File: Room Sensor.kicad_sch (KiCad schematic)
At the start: 15 parts, among them SW1 SW_Push, SW2 SW_Push, SW3 SW_Push, SW4 SW_Push, U2 ESP32-C3_SUPERMINI_TH

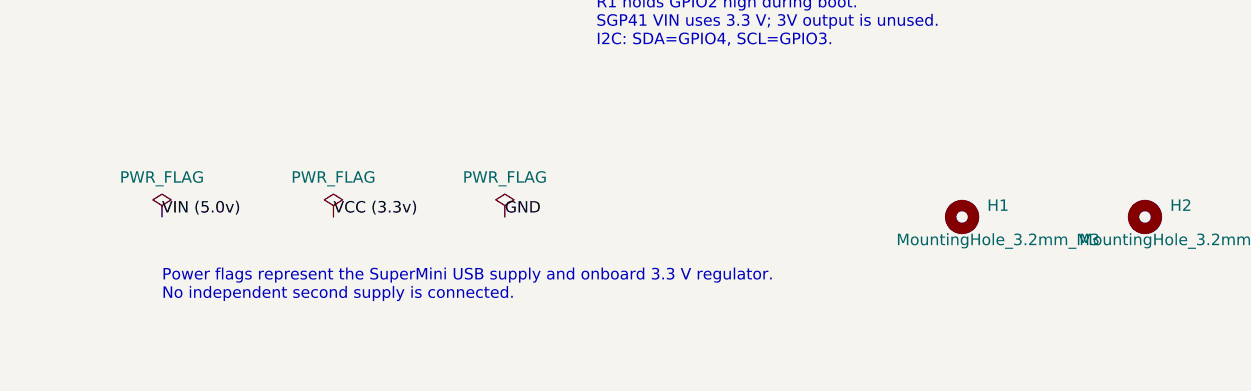
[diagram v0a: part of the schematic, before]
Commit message: Add KiCad latching USB power interface
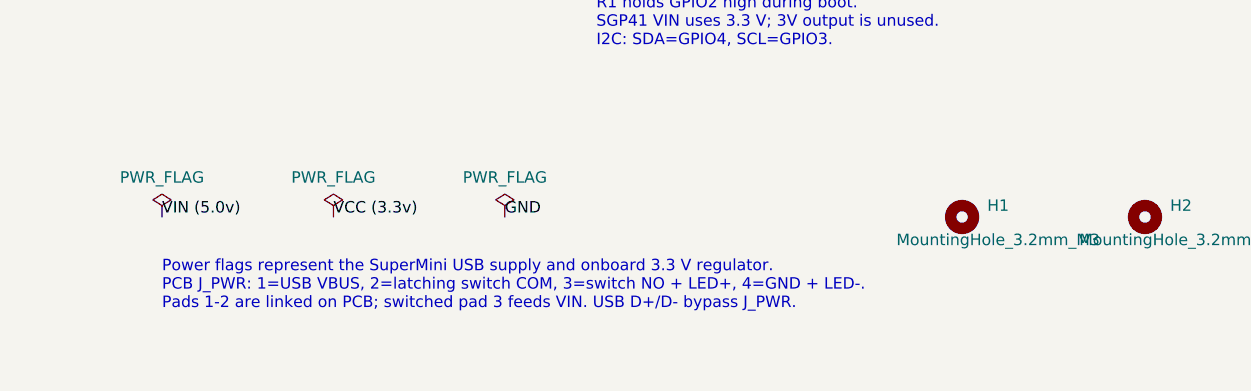
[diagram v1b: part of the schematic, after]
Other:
- note added: "Power flags represent the SuperMini USB supply and onboard 3.3 V regulator. PCB J_PWR: 1=USB VBUS, 2=latching switch COM, 3=switch NO + LED+, 4=GND + LED-. Pads 1-2 are linked on PCB; switched pad 3 feeds VIN. USB D+/D- bypass J_PWR."
- note removed: "Power flags represent the SuperMini USB supply and onboard 3.3 V regulator. No independent second supply is connected."
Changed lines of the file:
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@@
 		)
 	)
-	(text "Power flags represent the SuperMini USB supply and onboard 3.3 V regulator.\nNo independent second supply is connected."
+	(text "Power flags represent the SuperMini USB supply and onboard 3.3 V regulator.\nPCB J_PWR: 1=USB VBUS, 2=latching switch COM, 3=switch NO + LED+, 4=GND + LED-.\nPads 1-2 are linked on PCB; switched pad 3 feeds VIN. USB D+/D- bypass J_PWR."
 		(exclude_from_sim no)
 		(at 111.76 161.29 0)

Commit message: Add board-mounted USB-C power input
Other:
- note added: "Power flags represent the SuperMini USB supply and onboard 3.3 V regulator. PCB J_USB is a GCT USB4125 board-mounted 5 V power input; R_CC1/R_CC2 are 5.1 kOhm CC pull-downs. J_PWR: 1=raw VBUS, 2=latching switch COM, 3=switch NO + LED+, 4=GND + LED-. Pads 1-2 are linked; switched pad 3 feeds VIN. J_USB is power-only. Program through the ESP32-C3 SuperMini USB-C socket."
- note removed: "Power flags represent the SuperMini USB supply and onboard 3.3 V regulator. PCB J_PWR: 1=USB VBUS, 2=latching switch COM, 3=switch NO + LED+, 4=GND + LED-. Pads 1-2 are linked on PCB; switched pad 3 feeds VIN. USB D+/D- bypass J_PWR."
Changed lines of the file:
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@@
 		)
 	)
-	(text "Power flags represent the SuperMini USB supply and onboard 3.3 V regulator.\nPCB J_PWR: 1=USB VBUS, 2=latching switch COM, 3=switch NO + LED+, 4=GND + LED-.\nPads 1-2 are linked on PCB; switched pad 3 feeds VIN. USB D+/D- bypass J_PWR."
+	(text "Power flags represent the SuperMini USB supply and onboard 3.3 V regulator.\nPCB J_USB is a GCT USB4125 board-mounted 5 V power input; R_CC1/R_CC2 are 5.1 kOhm CC pull-downs.\nJ_PWR: 1=raw VBUS, 2=latching switch COM, 3=switch NO + LED+, 4=GND + LED-. Pads 1-2 are linked; switched pad 3 feeds VIN.\nJ_USB is power-only. Program through the ESP32-C3 SuperMini USB-C socket."
 		(exclude_from_sim no)
 		(at 111.76 161.29 0)
